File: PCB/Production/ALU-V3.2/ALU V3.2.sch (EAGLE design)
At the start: 85 parts, among them IC1 74ALS04N, IC10 74LS245N, IC11 74LS245N, IC12 74LS244N, IC13 74LS244N, IC14 74LS86N, IC15 74LS86N, IC16 74LS244N, IC17 74LS244N, IC18 74LS08N, IC19 74LS08N, IC2 74LS240N, IC20 74LS244N, IC21 74LS32N, IC22 74LS32N, IC23 74LS244N, IC24 74LS85N, IC25 74LS85N, IC26 74LS251N, IC27 74LS86N, IC28 74LS153N, IC29 74LS194N, IC3 74LS244N, IC30 74LS194N, IC31 74LS244N, IC32 74LS153N, IC33 74LS86N, IC34 74LS86N, IC35 74LS283N, IC36 74LS283N, IC37 74LS244N, IC4 74LS00N, IC5 74LS374N, IC6 74ALS08N, IC7 74LS32N, IC8 74LS138N, IC9 74LS74N, X1 FABC96R

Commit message: Next version of ALU to production
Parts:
- added JP2: (no value), pinhead:PINHD-1X3
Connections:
- removed net -BUS-OUT: IC10A.DIR, IC11A.DIR, IC1D.O
- removed net N$57: IC29A.QA, IC31A.A1, IC32A.1C1
- removed net N$74: IC30A.QD, IC31B.A4, IC32A.1C2
- new net N$10: IC27B.O, IC4B.I1
- new net N$15: IC1D.O, IC4B.I0
- new net N$16: IC1E.I, IC4B.O
- new net N$9: IC6C.I1, JP2.2
- new net SRD0: IC28A.2C1, IC29A.QA, IC31A.A1, IC32A.1C2
- new net SRD7: IC28A.1C1, IC30A.QD, IC31B.A4, IC32A.1C1
- net -AC-LD: now also JP2.1; no longer IC1D.I
- net -AC-RD: now also IC10A.DIR, IC11A.DIR
- net -ADD/SUB: now also IC1D.I
- net AC-LD: now also JP2.3; no longer IC6C.I1
- net ACO-DATA0: now also IC35A.A1; no longer IC28A.2C1, IC33A.I0
- net ACO-DATA1: now also IC35A.A2; no longer IC33B.I0
- net ACO-DATA2: now also IC35A.A3; no longer IC33C.I0
- net ACO-DATA3: now also IC35A.A4; no longer IC33D.I0
- net ACO-DATA4: now also IC36A.A1; no longer IC34A.I0
- net ACO-DATA5: now also IC36A.A2; no longer IC34B.I0
- net ACO-DATA6: now also IC36A.A3; no longer IC34C.I0
- net ACO-DATA7: now also IC36A.A4; no longer IC28A.1C1, IC34D.I0
- net BDATA0: now also IC33A.I0; no longer IC35A.A1
- net BDATA1: now also IC33B.I0; no longer IC35A.A2
- net BDATA2: now also IC33C.I0; no longer IC35A.A3
- net BDATA3: now also IC33D.I0; no longer IC35A.A4
- net BDATA4: now also IC34A.I0; no longer IC36A.A1
- net BDATA5: now also IC34B.I0; no longer IC36A.A2
- net BDATA6: now also IC34C.I0; no longer IC36A.A3
- net BDATA7: now also IC34D.I0; no longer IC36A.A4
- net CO/BO: now also IC1E.O; no longer IC27B.O
- net GND: no longer IC1E.I, IC4B.I0, IC4B.I1
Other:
- moved on the sheet: IC27B, IC6D

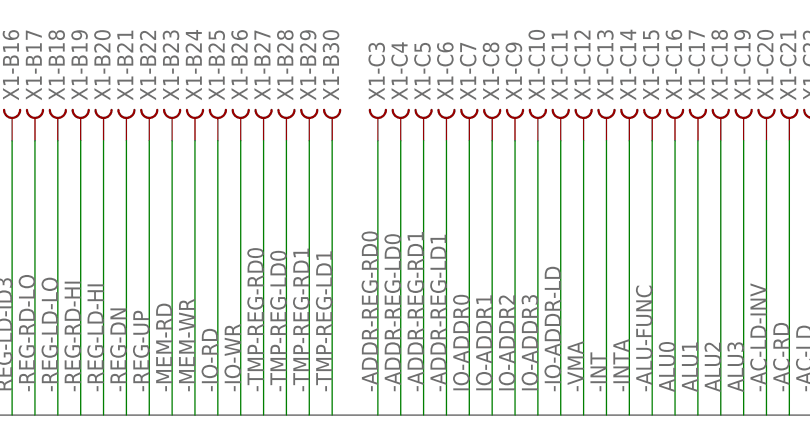
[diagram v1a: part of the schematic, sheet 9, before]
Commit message: Rename Connector C3-C6, ADDR-REG-ID0-3
Rename Connector C3-C6, ADDR-REG-ID0-3
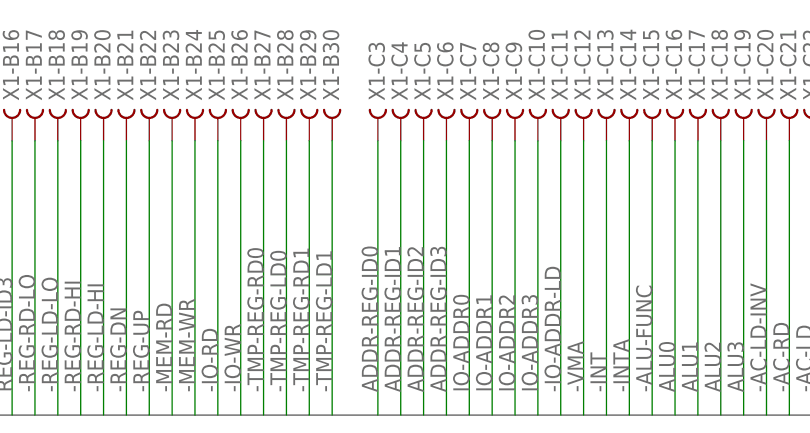
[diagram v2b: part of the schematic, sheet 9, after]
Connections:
- net -ADDR-REG-LD0 renamed ADDR-REG-ID1
- net -ADDR-REG-LD1 renamed ADDR-REG-ID3
- net -ADDR-REG-RD0 renamed ADDR-REG-ID0
- net -ADDR-REG-RD1 renamed ADDR-REG-ID2
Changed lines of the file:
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@@
 </segment>
 </net>
-<net name="-ADDR-REG-RD0" class="0">
+<net name="ADDR-REG-ID0" class="0">
 <segment>
 <pinref part="X1" gate="-C3" pin="B"/>
@@
 </segment>
 </net>
-<net name="-ADDR-REG-LD0" class="0">
+<net name="ADDR-REG-ID1" class="0">
 <segment>
 <pinref part="X1" gate="-C4" pin="B"/>
@@
 </segment>
 </net>
-<net name="-ADDR-REG-RD1" class="0">
+<net name="ADDR-REG-ID2" class="0">
 <segment>
 <pinref part="X1" gate="-C5" pin="B"/>
@@
 </segment>
 </net>
-<net name="-ADDR-REG-LD1" class="0">
+<net name="ADDR-REG-ID3" class="0">
 <segment>
 <pinref part="X1" gate="-C6" pin="B"/>
